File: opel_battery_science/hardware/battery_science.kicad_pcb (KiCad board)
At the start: 2 copper layers, 68.6 x 71.1 mm, 43 parts, among them P1 CONN_01X05, P2 CONN_01X01, P3 CONN_01X01, P4 CONN_01X01, P5 CONN_01X01, P6 CONN_01X06, P7 CONN_01X05, P8 CONN_01X05, SW1 SPST, SW2 SPST, U1 BQ76925, U2 LPC11C14, U3 SN74LV4051ADR

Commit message: Added external ADC, fixed power
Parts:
- removed P2, P3, P4, P5: CONN_01X01, bigConnection:BigConnection
- removed R7: R, Resistors_SMD:R_0603_HandSoldering
- added CREF1: 1μF, Capacitors_SMD:C_0603_HandSoldering, F.Cu at (157.5, 120.7)
- added Q1: BSS84, TO_SOT_Packages_SMD:SOT-23, F.Cu at (143.5, 100.3)
- added U4: MAX11612EUA+, Housings_SSOP:MSOP-8_3x3mm_Pitch0.65mm, F.Cu at (160.0, 129.5)
- P1: value CONN_01X05 -> CONN_01X08; footprint Pin_Headers:Pin_Header_Straight_1x05 -> Pin_Headers:Pin_Header_Straight_1x08
- moved P8 14.5 mm to (156.2, 146.1), turned to 270 degrees
- moved C12 14.2 mm to (152.4, 133.3), turned to 180 degrees
- moved C11 12.7 mm to (152.4, 128.3), turned to 180 degrees
- moved R6 11.7 mm to (147.3, 133.3)
- moved R5 9.25 mm to (142.2, 133.3)
- moved R1 9.16 mm to (142.2, 108.0), turned to 0 degrees
- moved C13 8.98 mm to (146.1, 128.3)
- moved R8 6.84 mm to (152.4, 123.2)
- moved U1 6.35 mm to (143.5, 120.7)
- moved C15 4.58 mm to (160.0, 106.7)
- moved P1 3.81 mm to (120.7, 129.5)
- moved C10 3.57 mm to (162.6, 139.7)
- moved U3 3.56 mm to (171.4, 141.0)
- moved C14 2.84 mm to (163.8, 110.5)
- moved C1 2.54 mm to (134.6, 102.9)
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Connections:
- net /A renamed /Thermistors/A
- net /ALERT renamed /BatteryMonitoring/ALERT
- net /B renamed /Thermistors/B
- net /C renamed /Thermistors/C
- net /INH renamed /Thermistors/INH
- net /LED0 renamed Net-(U2-Pad45)
- net /LED1 renamed Net-(U2-Pad9)
- net /PROGRAM renamed /microcontroller/PROGRAM
- net /RESET renamed /microcontroller/RESET
- net /RXD renamed /microcontroller/RXD
- net /SCL renamed /BatteryMonitoring/SCL
- net /SDA renamed /BatteryMonitoring/SDA
- net /TXD renamed /microcontroller/TXD
- C1 pad 1: /3.3V -> Net-(C1-Pad1)
- C10 pad 1: /THERM -> /BatteryMonitoring/COM
- C11 pad 1: /VCOUT -> /BatteryMonitoring/VCOUT
- C12 pad 1: /VIOUT -> /BatteryMonitoring/VIOUT
- C14 pad 1: /3.3V -> +3V3
- C15 pad 1: /3.3V -> +3V3
- C16 pad 1: /3.3V -> +3V3
- C17 pad 1: /3.3V -> +3V3
- C9 pad 1: /3.3V -> +3V3
- P1 pad 2: Net-(P1-Pad2) -> GND
- P6 pad 1: /3.3V -> +3V3
- R1 pad 1: /3.3V -> Net-(C1-Pad1)
- R11 pad 1: /3.3V -> +3V3
- R13 pad 1: /3.3V -> +3V3
- R14 pad 1: /3.3V -> +3V3
- R2 pad 1: /3.3V -> +3V3
- R3 pad 1: /3.3V -> +3V3
- R4 pad 1: /3.3V -> +3V3
- R6 pad 2: Net-(P2-Pad1) -> Net-(P1-Pad1)
- R8 pad 1: /THERM -> /BatteryMonitoring/COM
- RP1 pad 1: Net-(P3-Pad1) -> Net-(P1-Pad8)
- RP1 pad 16: /3.3V -> Net-(C1-Pad1)
- RP1 pad 2: Net-(P3-Pad1) -> Net-(P1-Pad8)
- RP1 pad 3: Net-(P1-Pad5) -> Net-(P1-Pad7)
- RP1 pad 4: Net-(P1-Pad4) -> Net-(P1-Pad6)
- RP1 pad 5: Net-(P1-Pad3) -> Net-(P1-Pad5)
- RP1 pad 6: Net-(P1-Pad2) -> Net-(P1-Pad4)
- RP1 pad 7: Net-(P1-Pad1) -> Net-(P1-Pad3)
- U1 pad 14: /VIOUT -> /BatteryMonitoring/VIOUT
- U1 pad 15: /VCOUT -> /BatteryMonitoring/VCOUT
- U1 pad 17: Net-(U1-Pad17) -> /BatteryMonitoring/VREF
- U1 pad 2: /3.3V -> Net-(C1-Pad1)
- U1 pad 20: /3.3V -> +3V3
- U2 pad 32: /THERM -> Net-(U2-Pad32)
- U2 pad 33: /VCOUT -> Net-(U2-Pad33)
- U2 pad 34: /VIOUT -> Net-(U2-Pad34)
- U2 pad 44: /3.3V -> +3V3
- U2 pad 8: /3.3V -> +3V3
- U3 pad 16: /3.3V -> +3V3
- U3 pad 3: /THERM -> /BatteryMonitoring/COM
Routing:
- net /3.3V: track 173.3 -> 0.00 mm, vias 3 -> 0
- net +3V3: track 0.00 -> 148.4 mm, vias 0 -> 5
- net GND: track 99.4 -> 44.5 mm, vias 15 -> 16
- net Net-(P2-Pad1): track 52.0 -> 0.00 mm
- net Net-(C1-Pad1): track 0.00 -> 49.6 mm
- net /THERM: track 35.0 -> 0.00 mm, vias 2 -> 0
- net /BatteryMonitoring/COM: track 0.00 -> 28.8 mm, vias 0 -> 2
- net Net-(P3-Pad1): track 28.1 -> 0.00 mm
- net Net-(P1-Pad1): track 9.40 -> 37.2 mm
- net /VIOUT: track 25.9 -> 0.00 mm
- net /VCOUT: track 25.1 -> 0.00 mm
- net /BatteryMonitoring/VREF: track 0.00 -> 23.3 mm
- net /BatteryMonitoring/ALERT: track 39.4 -> 61.8 mm, vias 3 -> 2
- net /BatteryMonitoring/VIOUT: track 0.00 -> 21.5 mm
- net /BatteryMonitoring/SCL: track 15.2 -> 36.4 mm, vias 0 -> 2
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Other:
- board size 68.6 x 71.1 mm -> 68.6 x 62.2 mm

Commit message: Swapped out ADC part number
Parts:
- U4: value MAX11612EUA+ -> MAX11613EUA+
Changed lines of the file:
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@@
       (effects (font (size 1 1) (thickness 0.15)))
     )
-    (fp_text value MAX11612EUA+ (at 0 2.6) (layer F.Fab)
+    (fp_text value MAX11613EUA+ (at 0 2.6) (layer F.Fab)
       (effects (font (size 1 1) (thickness 0.15)))
     )
@@
   (segment (start 136.21 138.43) (end 136.21 138.75) (width 0.25) (layer F.Cu) (net 0))
   (segment (start 136.21 113.03) (end 136.21 112.71) (width 0.25) (layer F.Cu) (net 0))
-  (segment (start 158.43 120.65) (end 158.43 122.87) (width 0.25) (layer F.Cu) (net 1) (status 400000))
+  (segment (start 158.43 120.65) (end 158.43 122.87) (width 0.25) (layer F.Cu) (net 1))
   (via (at 158.496 122.936) (size 0.6) (drill 0.4) (layers F.Cu B.Cu) (net 1))
   (segment (start 158.43 122.87) (end 158.496 122.936) (width 0.25) (layer F.Cu) (net 1))
@@
   (segment (start 162.588 118.9) (end 164.56 118.9) (width 0.25) (layer F.Cu) (net 68))
   (segment (start 162.063 118.375) (end 162.588 118.9) (width 0.25) (layer F.Cu) (net 68))
-  (segment (start 156.53 120.65) (end 156.53 123.764) (width 0.25) (layer F.Cu) (net 69) (status 400000))
+  (segment (start 156.53 120.65) (end 156.53 123.764) (width 0.25) (layer F.Cu) (net 69))
   (segment (start 159.299 130.515) (end 159.512 130.302) (width 0.25) (layer F.Cu) (net 69))
   (segment (start 159.512 130.302) (end 159.512 126.746) (width 0.25) (layer F.Cu) (net 69))
@@
   (segment (start 156.53 123.764) (end 159.004 126.238) (width 0.25) (layer F.Cu) (net 69))
   (segment (start 152.4 119.634) (end 153.67 119.634) (width 0.25) (layer F.Cu) (net 69))
-  (segment (start 154.686 120.65) (end 156.53 120.65) (width 0.25) (layer F.Cu) (net 69) (status 800000))
+  (segment (start 154.686 120.65) (end 156.53 120.65) (width 0.25) (layer F.Cu) (net 69))
   (segment (start 153.67 119.634) (end 154.686 120.65) (width 0.25) (layer F.Cu) (net 69))
   (segment (start 152.4 119.634) (end 152.441 119.675) (width 0.25) (layer F.Cu) (net 69))

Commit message: Many fixes, corrected schematic, roughly tried to partition board
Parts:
- removed C1: 10μF, Capacitors_SMD:C_0603_HandSoldering
- removed C10: C, Capacitors_SMD:C_0603_HandSoldering
- removed C11, C13, C14, C17: .1μF, Capacitors_SMD:C_0603_HandSoldering
- removed C12: 1nF, Capacitors_SMD:C_0603_HandSoldering
- removed C15, C16: 1μF, Capacitors_SMD:C_0805_HandSoldering
- removed C2, C3, C4, C5, C6, C7, C8, CREF1: 1μF, Capacitors_SMD:C_0603_HandSoldering
- removed C9: 4.7μF, Capacitors_SMD:C_0603_HandSoldering
- removed D3: LED, LEDs:LED_0805
- removed P1: CONN_01X08, Pin_Headers:Pin_Header_Straight_1x08
- removed P6: CONN_01X06, Pin_Headers:Pin_Header_Straight_1x06
- removed P7, P8: CONN_01X05, Pin_Headers:Pin_Header_Straight_1x05
- removed Q1: BSS84, TO_SOT_Packages_SMD:SOT-23
- removed R1: 200k, Resistors_SMD:R_0603_HandSoldering
- removed R11: 100, Resistors_SMD:R_0603_HandSoldering
- removed R13, R14, R8: 10k, Resistors_SMD:R_0603_HandSoldering
- removed R2, R3, R4: 4.7k, Resistors_SMD:R_0603_HandSoldering
- removed R5, R6: 1k, Resistors_SMD:R_0603_HandSoldering
- removed RP1: CAY16-101J8LF, Resistors_SMD:R_Cat16-8
- removed SW1: SPST, Buttons_Switches_ThroughHole:SW_Micro_SPST
- removed SW2: SPST, Buttons_Switches_SMD:SW_SPST_EVPBF
- removed U1: BQ76925, Housings_SSOP:TSSOP-20_4.4x6.5mm_Pitch0.65mm
- removed U2: LPC11C14, Housings_QFP:LQFP-48_7x7mm_Pitch0.5mm
- removed U3: SN74LV4051ADR, Housings_SOIC:SOIC-16_3.9x9.9mm_Pitch1.27mm
- removed U4: MAX11613EUA+, Housings_SSOP:MSOP-8_3x3mm_Pitch0.65mm
- added C201: .1μF, Capacitors_SMD:C_0603_HandSoldering, F.Cu at (161.3, 101.6)
- added C202: 1μF, Capacitors_SMD:C_0805_HandSoldering, F.Cu at (156.2, 101.6)
- added C301: 10μF, Capacitors_SMD:C_0603_HandSoldering, F.Cu at (136.1, 112.5)
- added C302: 1μF, Capacitors_SMD:C_0603_HandSoldering, F.Cu at (136.1, 116.3)
- added C303: 1μF, Capacitors_SMD:C_0603_HandSoldering, F.Cu at (136.1, 120.1)
- added C304: 1μF, Capacitors_SMD:C_0603_HandSoldering, F.Cu at (136.1, 124.0)
- added C305: 1μF, Capacitors_SMD:C_0603_HandSoldering, F.Cu at (136.1, 127.8)
- added C306: 1μF, Capacitors_SMD:C_0603_HandSoldering, F.Cu at (136.1, 131.6)
- added C307: 1μF, Capacitors_SMD:C_0603_HandSoldering, F.Cu at (136.1, 135.4)
- added C308: 1μF, Capacitors_SMD:C_0603_HandSoldering, F.Cu at (136.1, 139.2)
- added C309: .1μF, Capacitors_SMD:C_0603_HandSoldering, F.Cu at (147.3, 130.8)
- added C310: 4.7μF, Capacitors_SMD:C_0603_HandSoldering, F.Cu at (151.1, 113.0)
- added C311: .1μF, Capacitors_SMD:C_0603_HandSoldering, F.Cu at (175.4, 125.9)
- added C312: .1μF, Capacitors_SMD:C_0603_HandSoldering, F.Cu at (153.7, 125.7)
- added C313: 1nF, Capacitors_SMD:C_0603_HandSoldering, F.Cu at (153.7, 130.8)
- added C314: .1μF, Capacitors_SMD:C_0603_HandSoldering, F.Cu at (175.4, 129.7)
- added C315: .1μF, Capacitors_SMD:C_0603_HandSoldering, F.Cu at (175.4, 133.5)
- added C316: .1μF, Capacitors_SMD:C_0603_HandSoldering, F.Cu at (175.4, 137.3)
- added C317: .1μF, Capacitors_SMD:C_0603_HandSoldering, F.Cu at (175.4, 141.1)
- added C320: 1μF, Capacitors_SMD:C_0603_HandSoldering, F.Cu at (153.7, 120.7)
- added C401: 100nF, Capacitors_SMD:C_0603_HandSoldering, F.Cu at (157.5, 119.4)
- added C402: 100nF, Capacitors_SMD:C_0603_HandSoldering, F.Cu at (162.6, 119.4)
- added D201: LED, LEDs:LED_0805, F.Cu at (172.7, 115.6)
- added P201: CONN_01X06, Pin_Headers:Pin_Header_Straight_1x06, F.Cu at (179.1, 116.8)
- added P301: CONN_01X08, Pin_Headers:Pin_Header_Straight_1x08, F.Cu at (124.5, 132.1)
- added P401: CONN_01X05, Pin_Headers:Pin_Header_Straight_1x05, F.Cu at (168.9, 128.3)
- added P402: CONN_01X05, Pin_Headers:Pin_Header_Straight_1x05, F.Cu at (163.8, 138.4)
- added Q301: BSS84, TO_SOT_Packages_SMD:SOT-23, F.Cu at (146.1, 110.5)
- added R201: 100, Resistors_SMD:R_0603_HandSoldering, F.Cu at (172.7, 120.7)
- added R202: 10k, Resistors_SMD:R_0603_HandSoldering, F.Cu at (141.0, 106.7)
- added R203: 10k, Resistors_SMD:R_0603_HandSoldering, F.Cu at (135.9, 106.7)
- added R301: 1k, Resistors_SMD:R_0603_HandSoldering, F.Cu at (144.8, 134.6)
- added R302: 200k, Resistors_SMD:R_0603_HandSoldering, F.Cu at (147.3, 116.8)
- added R303: 1k, Resistors_SMD:R_0603_HandSoldering, F.Cu at (149.9, 134.6)
- added R305: 4.7k, Resistors_SMD:R_0603_HandSoldering, F.Cu at (157.5, 115.6)
- added R306: 4.7k, Resistors_SMD:R_0603_HandSoldering, F.Cu at (154.9, 105.4)
- added R307: 4.7k, Resistors_SMD:R_0603_HandSoldering, F.Cu at (152.4, 109.2)
- added R308: 10k, Resistors_SMD:R_0603_HandSoldering, F.Cu at (180.5, 125.9)
- added R309: 10k, Resistors_SMD:R_0603_HandSoldering, F.Cu at (180.5, 129.7)
- added R310: 10k, Resistors_SMD:R_0603_HandSoldering, F.Cu at (180.5, 133.5)
- added R311: 10k, Resistors_SMD:R_0603_HandSoldering, F.Cu at (180.5, 137.3)
- added R312: 10k, Resistors_SMD:R_0603_HandSoldering, F.Cu at (180.5, 141.1)
- added RP101: 47Ω, Resistors_SMD:R_Array_Convex_8x0602, F.Cu at (167.6, 119.4)
- added RP301: CAY16-101J8LF, Resistors_SMD:R_Cat16-8, F.Cu at (129.5, 125.7)
- added SW201: SPST, Buttons_Switches_ThroughHole:SW_Micro_SPST, F.Cu at (147.3, 104.1)
- added SW202: SPST, Buttons_Switches_SMD:SW_SPST_EVPBF, F.Cu at (128.3, 105.4)
- added U201: LPC11C14, Housings_QFP:LQFP-48_7x7mm_Pitch0.5mm, F.Cu at (165.1, 109.2)
- added U301: BQ76925, Housings_SSOP:TSSOP-20_4.4x6.5mm_Pitch0.65mm, F.Cu at (147.3, 124.5)
- added U401: ADS1148IPWR, Housings_SSOP:TSSOP-28_4.4x9.7mm_Pitch0.65mm, F.Cu at (161.3, 127.0)
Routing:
- net Net-(C1-Pad1): track 49.6 -> 0.00 mm
- net Net-(C301-Pad1): track 0.00 -> 42.9 mm
- net Net-(C8-Pad1): track 41.5 -> 0.00 mm
- net Net-(P1-Pad1): track 37.2 -> 0.00 mm
- net Net-(C308-Pad1): track 0.00 -> 32.6 mm
- net Net-(C7-Pad1): track 32.2 -> 0.00 mm
- net Net-(C2-Pad1): track 31.6 -> 0.00 mm
- net Net-(P301-Pad1): track 0.00 -> 31.0 mm
- net Net-(C307-Pad1): track 0.00 -> 29.3 mm
- net /BatteryMonitoring/COM: track 28.8 -> 0.00 mm, vias 2 -> 0
- net /BatteryMonitoring/ALERT: track 61.8 -> 33.7 mm
- net /ADC/Thermistors/TH5: track 0.00 -> 27.0 mm
- net /Thermistors/C: track 26.9 -> 0.00 mm
- net /Thermistors/B: track 26.4 -> 0.00 mm
- net /Thermistors/A: track 25.7 -> 0.00 mm
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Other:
- board size 68.6 x 62.2 mm -> 61 x 44.5 mm
- board text added: "GND"
- board text removed: "Battery Analysis - August 5th, 2016"
- board text removed: "MODE"
- board text removed: "Measurement Connections"
- board text removed: "Thermistor +"
- board text removed: "Thermistor GND"

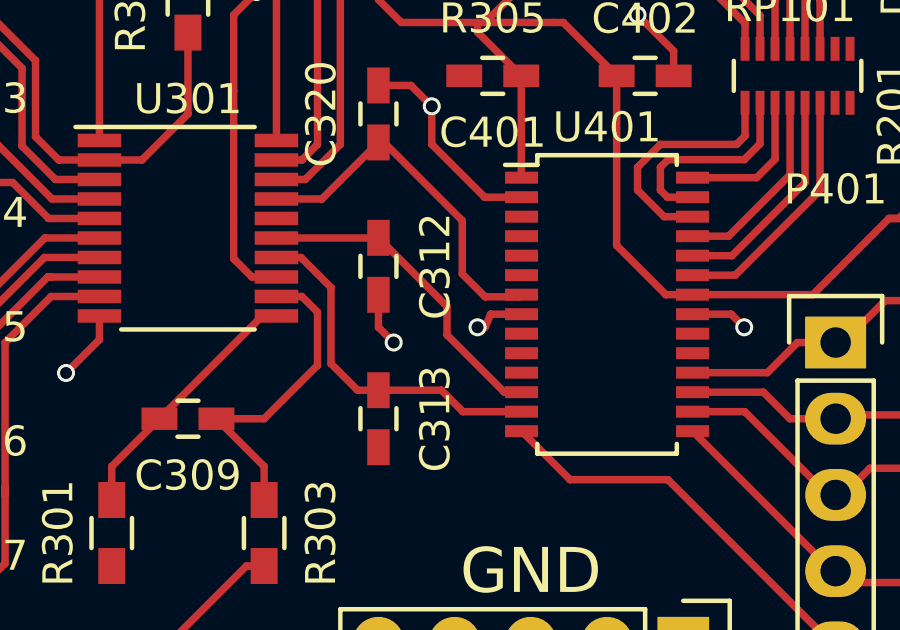
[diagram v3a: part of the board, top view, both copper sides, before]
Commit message: Added ground connection for differnetial input
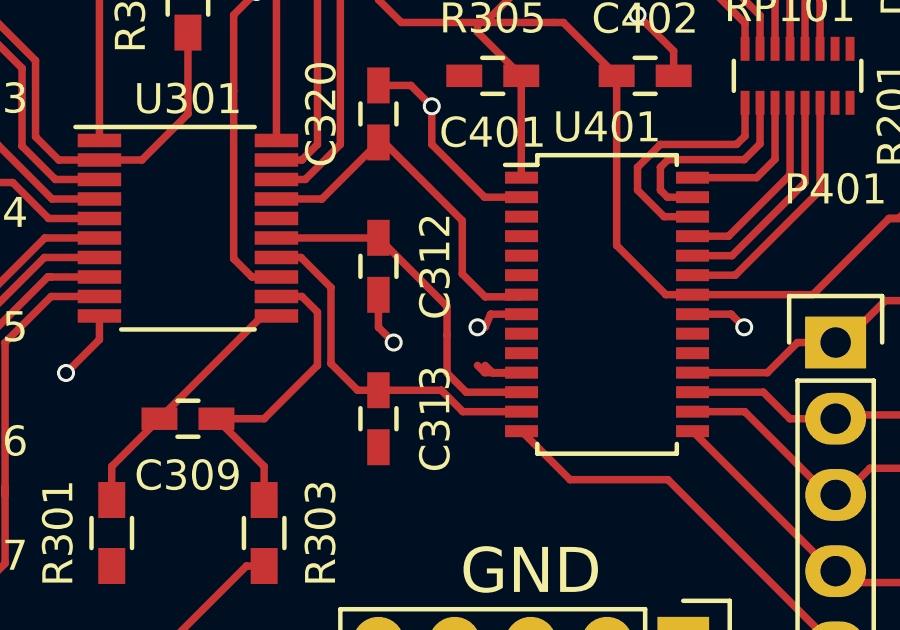
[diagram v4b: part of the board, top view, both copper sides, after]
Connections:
- U401 pad 11: Net-(U401-Pad11) -> GND
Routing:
- net GND: track 64.1 -> 67.0 mm
- net /ADC/Thermistors/VCOUT: track 10.9 -> 11.7 mm
